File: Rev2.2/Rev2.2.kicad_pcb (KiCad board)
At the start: 4 copper layers, 91.8 x 94.5 mm, 119 parts, among them J1 Termination, J10 USART1, J11 3.3V power breakout, J12 5V power breakout, J13 AIN1, J15 USART6, J16 AIN2, J17 AIN3, J18 AIN4, J2 CAN2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

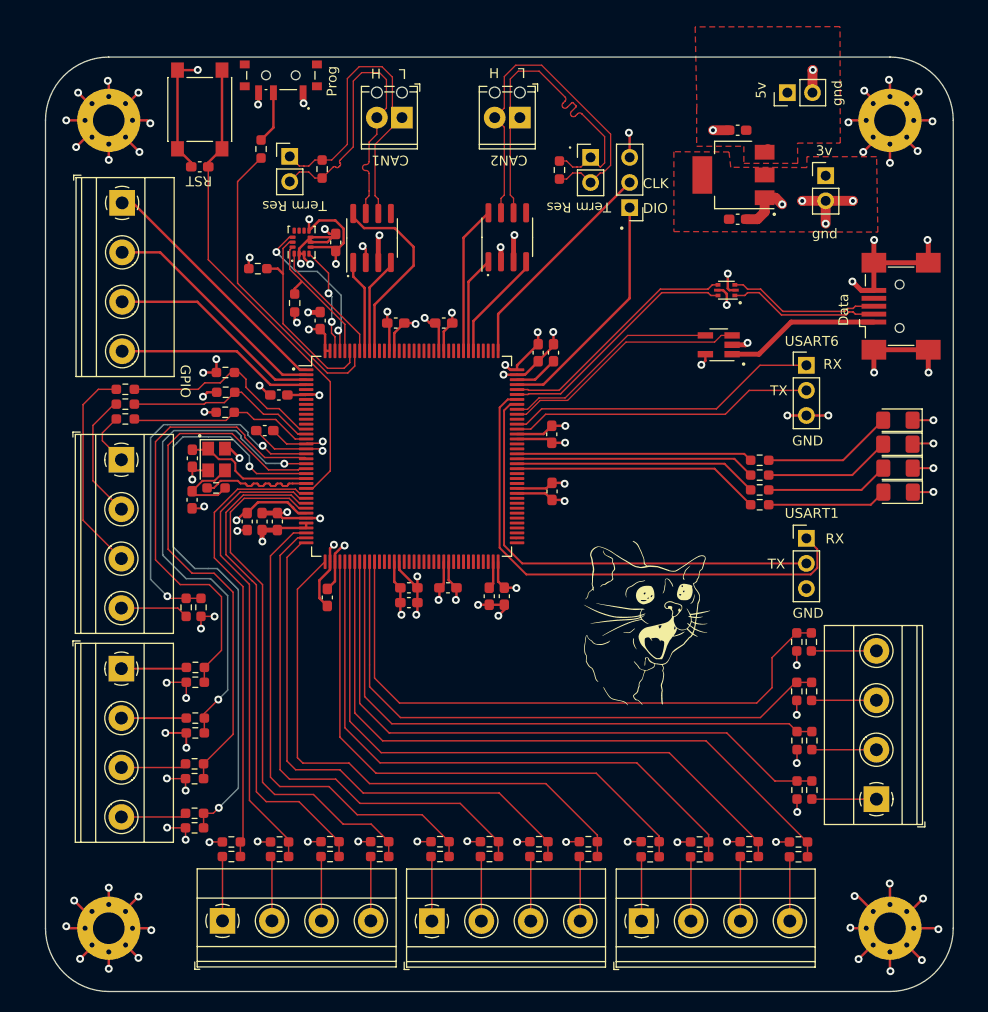
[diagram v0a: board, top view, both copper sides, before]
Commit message: changed layer stack up to sig,gnd,gnd, sig/power and routing according to the new stackup
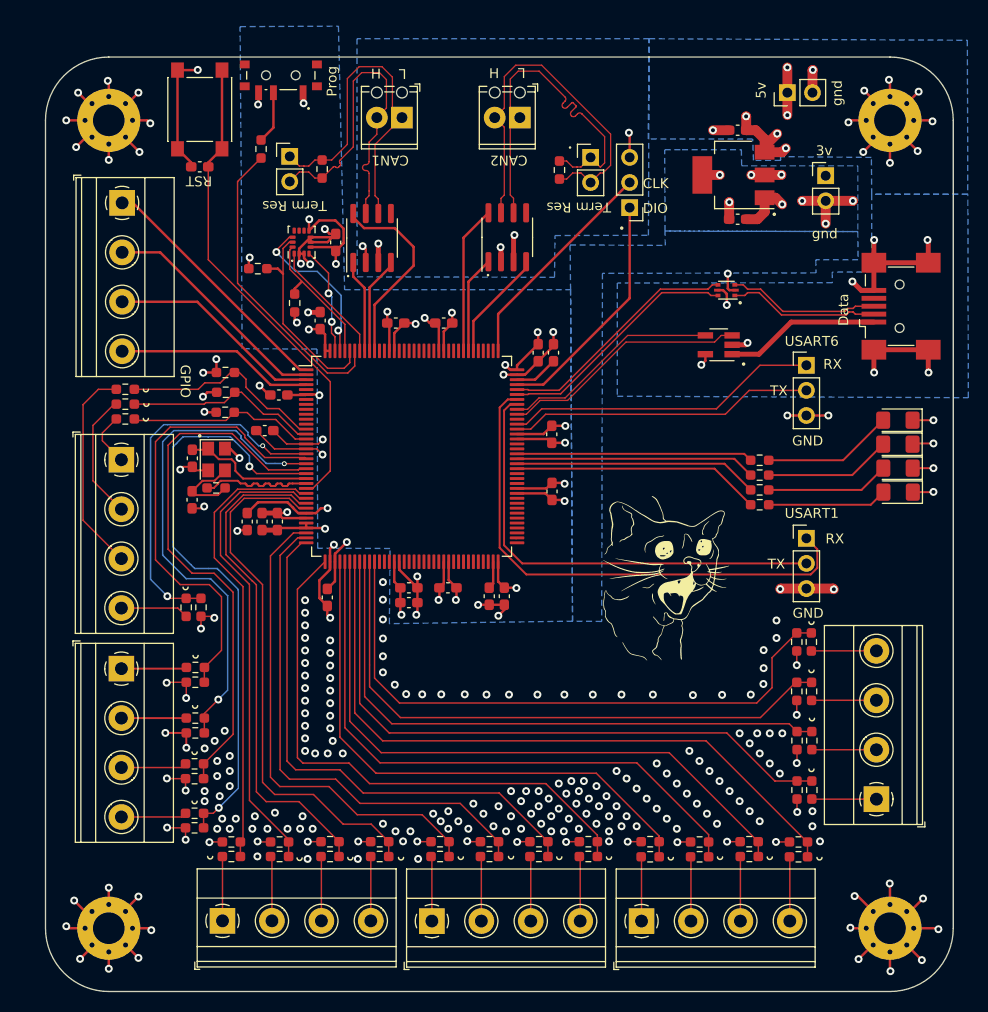
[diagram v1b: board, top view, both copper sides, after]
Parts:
- moved G*** 4.93 mm to (163.6, 111.0)
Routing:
- net +5V: track 9.48 -> 22.6 mm, vias 4 -> 9
- net +3.3V: track 91.0 -> 100.2 mm, vias 21 -> 25
- net GND: track 269.0 -> 274.5 mm, vias 109 -> 272
- added copper zone on B.Cu, net +3.3V
- added copper zone on B.Cu, net +5V
- removed copper zone on F.Cu, net +3.3V
- removed copper zone on F.Cu, net +5V
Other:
- board text added: "Analog section"
- board text added: "USB and UART"
- board text removed: "USB"

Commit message: added a usb C for power delivery and moved voltage regulator and readjusted the partial power plane to fit the USB C
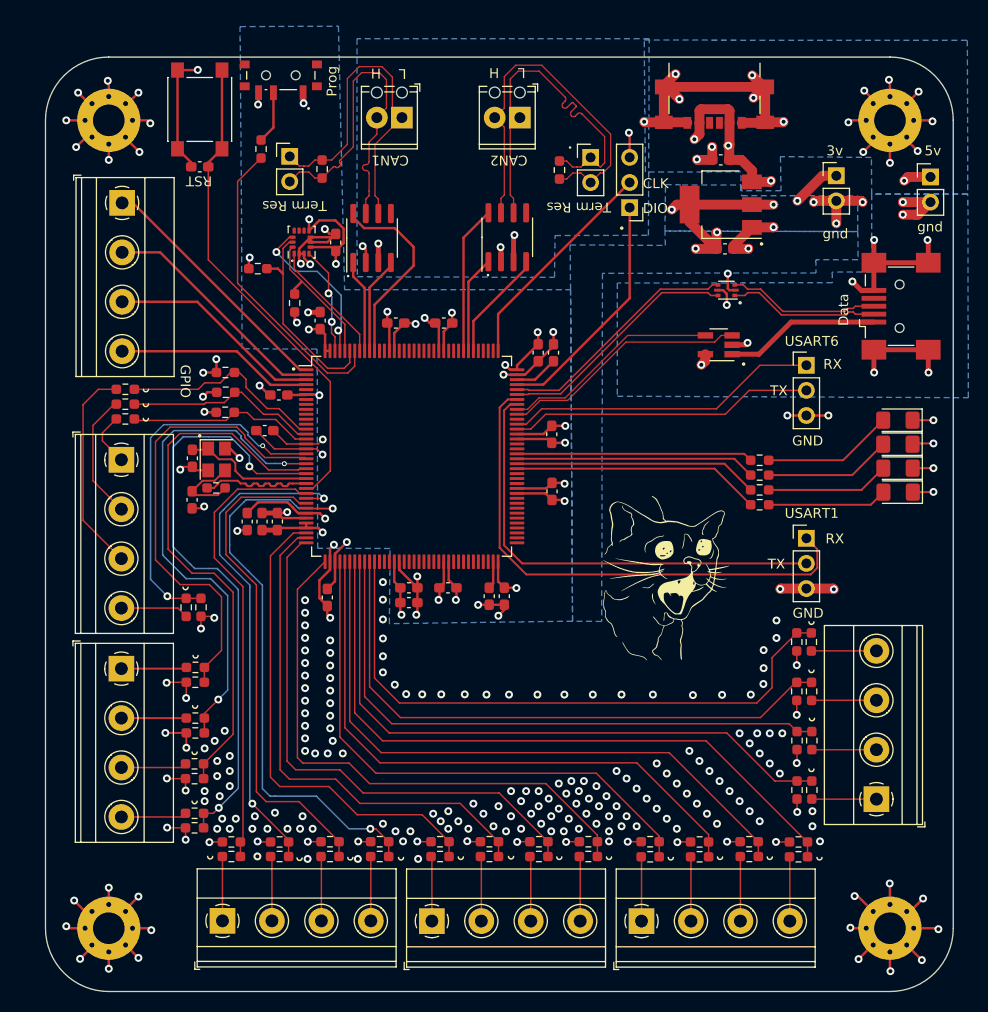
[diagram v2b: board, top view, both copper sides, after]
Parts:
- added J14: USB C PWR, Connector_USB:USB_C_Receptacle_GCT_USB4135-GF-A_6P_TopMnt_Horizontal, F.Cu at (168.7, 61.7)
- moved J12 16.8 mm to (190.5, 70.2), turned to 0 degrees
- moved C26 3.45 mm to (169.3, 68.5)
- moved C32 3.26 mm to (169.7, 77.5)
- moved U3 3.26 mm to (169.3, 73.0)
- moved J11 1.08 mm to (181.0, 70.1)
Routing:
- net GND: track 274.5 -> 313.9 mm, vias 272 -> 281
- net +3.3V: track 100.2 -> 118.2 mm, vias 25 -> 26
- net +5V: track 22.6 -> 28.2 mm, vias 9 -> 8
- net A12: track 54.1 -> 59.6 mm, vias 0 -> 2
- net A10: track 47.5 -> 51.0 mm, vias 0 -> 2

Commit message: added manufacturing files
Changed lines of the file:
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@@
       (outputformat 1)
       (mirror false)
-      (drillshape 1)
+      (drillshape 0)
       (scaleselection 1)
-      (outputdirectory "")
+      (outputdirectory "manufacturing/")
     )
   )
@@
     (fp_line (start 1.6 0.8) (end 1.6 -0.8)
       (stroke (width 0.1) (type solid)) (layer "F.Fab"))
-    (pad "1" smd roundrect (at -1.4875 0 180) (size 1.425 1.75) (layers "F.Cu" "F.Paste" "F.Mask") (roundrect_rratio 0.175439)
+    (pad "1" smd roundrect (at -1.4875 0 180) (size 1.425 1.75) (layers "F.Cu" "F.Paste" "F.Mask") (roundrect_rratio 0.1754392982)
       (net 2 "GND") (pinfunction "K") (pintype "passive"))
-    (pad "2" smd roundrect (at 1.4875 0 180) (size 1.425 1.75) (layers "F.Cu" "F.Paste" "F.Mask") (roundrect_rratio 0.175439)
+    (pad "2" smd roundrect (at 1.4875 0 180) (size 1.425 1.75) (layers "F.Cu" "F.Paste" "F.Mask") (roundrect_rratio 0.1754392982)
       (net 4 "Net-(D2-A)") (pinfunction "A") (pintype "passive"))
     (model "${KICAD6_3DMODEL_DIR}/LED_SMD.3dshapes/LED_1206_3216Metric.wrl"
@@
     (fp_line (start 1.6 0.8) (end 1.6 -0.8)
       (stroke (width 0.1) (type solid)) (layer "F.Fab"))
-    (pad "1" smd roundrect (at -1.4875 0 180) (size 1.425 1.75) (layers "F.Cu" "F.Paste" "F.Mask") (roundrect_rratio 0.175439)
+    (pad "1" smd roundrect (at -1.4875 0 180) (size 1.425 1.75) (layers "F.Cu" "F.Paste" "F.Mask") (roundrect_rratio 0.1754392982)
       (net 2 "GND") (pinfunction "K") (pintype "passive"))
-    (pad "2" smd roundrect (at 1.4875 0 180) (size 1.425 1.75) (layers "F.Cu" "F.Paste" "F.Mask") (roundrect_rratio 0.175439)
+    (pad "2" smd roundrect (at 1.4875 0 180) (size 1.425 1.75) (layers "F.Cu" "F.Paste" "F.Mask") (roundrect_rratio 0.1754392982)
       (net 5 "Net-(D3-A)") (pinfunction "A") (pintype "passive"))
     (model "${KICAD6_3DMODEL_DIR}/LED_SMD.3dshapes/LED_1206_3216Metric.wrl"
@@
     (fp_line (start 1.6 0.8) (end 1.6 -0.8)
       (stroke (width 0.1) (type solid)) (layer "F.Fab"))
-    (pad "1" smd roundrect (at -1.4875 0 180) (size 1.425 1.75) (layers "F.Cu" "F.Paste" "F.Mask") (roundrect_rratio 0.175439)
+    (pad "1" smd roundrect (at -1.4875 0 180) (size 1.425 1.75) (layers "F.Cu" "F.Paste" "F.Mask") (roundrect_rratio 0.1754392982)
       (net 2 "GND") (pinfunction "K") (pintype "passive"))
-    (pad "2" smd roundrect (at 1.4875 0 180) (size 1.425 1.75) (layers "F.Cu" "F.Paste" "F.Mask") (roundrect_rratio 0.175439)
+    (pad "2" smd roundrect (at 1.4875 0 180) (size 1.425 1.75) (layers "F.Cu" "F.Paste" "F.Mask") (roundrect_rratio 0.1754392982)
       (net 6 "Net-(D4-A)") (pinfunction "A") (pintype "passive"))
     (model "${KICAD6_3DMODEL_DIR}/LED_SMD.3dshapes/LED_1206_3216Metric.wrl"
@@
     (fp_line (start 1.6 0.8) (end 1.6 -0.8)
       (stroke (width 0.1) (type solid)) (layer "F.Fab"))
-    (pad "1" smd roundrect (at -1.4875 0 180) (size 1.425 1.75) (layers "F.Cu" "F.Paste" "F.Mask") (roundrect_rratio 0.175439)
+    (pad "1" smd roundrect (at -1.4875 0 180) (size 1.425 1.75) (layers "F.Cu" "F.Paste" "F.Mask") (roundrect_rratio 0.1754392982)
       (net 2 "GND") (pinfunction "K") (pintype "passive"))
-    (pad "2" smd roundrect (at 1.4875 0 180) (size 1.425 1.75) (layers "F.Cu" "F.Paste" "F.Mask") (roundrect_rratio 0.175439)
+    (pad "2" smd roundrect (at 1.4875 0 180) (size 1.425 1.75) (layers "F.Cu" "F.Paste" "F.Mask") (roundrect_rratio 0.1754392982)
       (net 3 "Net-(D1-A)") (pinfunction "A") (pintype "passive"))
     (model "${KICAD6_3DMODEL_DIR}/LED_SMD.3dshapes/LED_1206_3216Metric.wrl"
@@
   (gr_circle (center 168.9608 138.7348) (end 168.9608 138.7348)
     (stroke (width 0.15) (type default)) (fill none) (layer "F.SilkS"))
+  (gr_line (start 189.992 98.552) (end 190.4492 98.552)
+    (stroke (width 0.15) (type default)) (layer "F.SilkS"))
   (gr_circle (center 154.05 67.25) (end 154 67.25)
     (stroke (width 0.15) (type default)) (fill none) (layer "F.SilkS"))
@@
   (gr_arc (start 164.4904 139.0396) (mid 164.2364 139.2936) (end 163.9824 139.0396)
     (stroke (width 0.15) (type default)) (layer "F.SilkS"))
+  (gr_line (start 189.9793 96.139) (end 190.4619 96.139)
+    (stroke (width 0.15) (type default)) (layer "F.SilkS"))
   (gr_arc (start 116.332 128.3716) (mid 116.078 128.6256) (end 115.824 128.3716)
     (stroke (width 0.15) (type default)) (layer "F.SilkS"))
@@
   (gr_circle (center 117.3988 138.684) (end 117.3988 138.684)
     (stroke (width 0.15) (type default)) (fill none) (layer "F.SilkS"))
+  (gr_line (start 189.9793 100.9904) (end 190.4619 100.9904)
+    (stroke (width 0.15) (type default)) (layer "F.SilkS"))
   (gr_circle (center 147.828 138.684) (end 147.828 138.684)
     (stroke (width 0.15) (type default)) (fill none) (layer "F.SilkS"))
@@
   (gr_circle (center 164.4904 138.7856) (end 164.4904 138.7856)
     (stroke (width 0.15) (type default)) (fill none) (layer "F.SilkS"))
+  (gr_line (start 189.992 93.726) (end 190.4746 93.726)
+    (stroke (width 0.15) (type default)) (layer "F.SilkS"))
   (gr_arc (start 143.256 138.9888) (mid 143.002 139.2428) (end 142.748 138.9888)
     (stroke (width 0.15) (type default)) (layer "F.SilkS"))

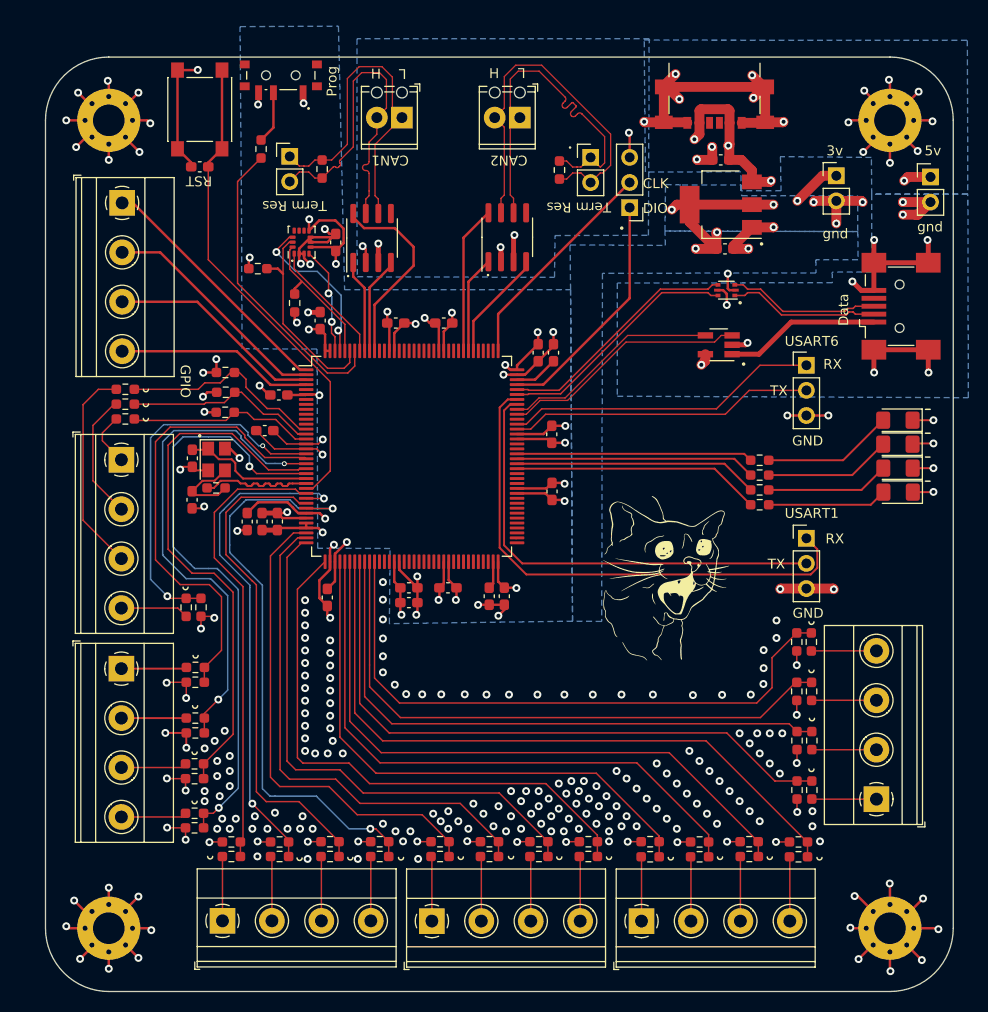
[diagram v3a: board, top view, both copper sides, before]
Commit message: updated gerber files to reflect some partial power plane adjustments
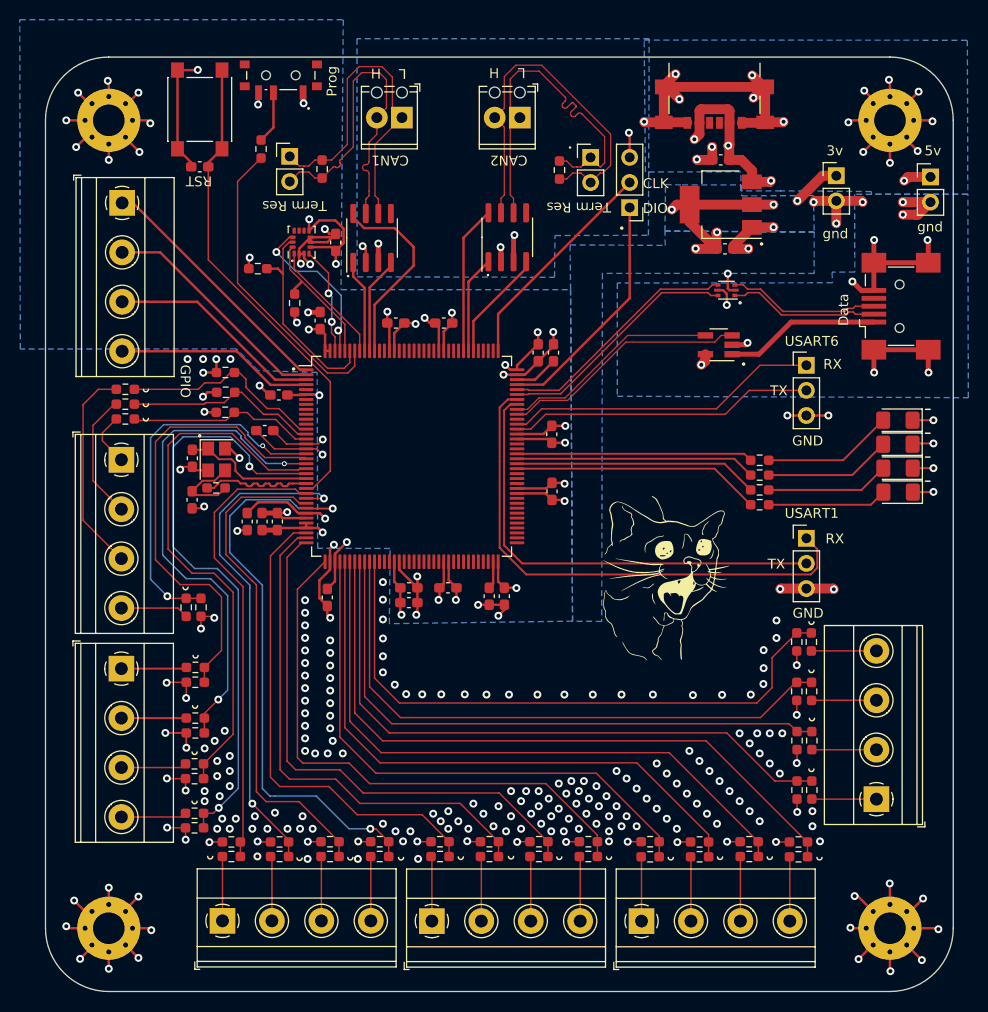
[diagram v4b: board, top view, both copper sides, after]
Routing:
- net GND: vias 281 -> 284
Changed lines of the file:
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@@
   (via (at 147.875 122.575) (size 0.8) (drill 0.4) (layers "F.Cu" "B.Cu") (net 2))
   (via (at 118.364 129.286) (size 0.8) (drill 0.4) (layers "F.Cu" "B.Cu") (net 2))
+  (via (at 119.7102 88.646) (size 0.8) (drill 0.4) (layers "F.Cu" "B.Cu") (net 2))
   (via (at 179.324 137.414) (size 0.8) (drill 0.4) (layers "F.Cu" "B.Cu") (net 2))
   (via (at 137 114.5) (size 0.8) (drill 0.4) (layers "F.Cu" "B.Cu") (net 2))
@@
   (via (at 119.634 128.778) (size 0.8) (drill 0.4) (layers "F.Cu" "B.Cu") (net 2))
   (via (at 159.25 122.575) (size 0.8) (drill 0.4) (layers "F.Cu" "B.Cu") (net 2))
+  (via (at 116.9416 88.646) (size 0.8) (drill 0.4) (layers "F.Cu" "B.Cu") (net 2))
   (via (at 142.748 135.382) (size 0.8) (drill 0.4) (layers "F.Cu" "B.Cu") (net 2))
   (via (at 127.254 114.3) (size 0.8) (drill 0.4) (layers "F.Cu" "B.Cu") (net 2))
@@
   (via (at 180.975 74.93) (size 0.8) (drill 0.4) (layers "F.Cu" "B.Cu") (net 2))
   (via (at 146.812 133.858) (size 0.8) (drill 0.4) (layers "F.Cu" "B.Cu") (net 2))
+  (via (at 115.3668 88.646) (size 0.8) (drill 0.4) (layers "F.Cu" "B.Cu") (net 2))
   (via (at 119.634 131.826) (size 0.8) (drill 0.4) (layers "F.Cu" "B.Cu") (net 2))
   (via (at 155.956 133.096) (size 0.8) (drill 0.4) (layers "F.Cu" "B.Cu") (net 2))
@@
     (polygon
       (pts
-        (xy 130.625 54.975)
-        (xy 131.25 81.625)
+        (xy 131.1148 54.3306)
+        (xy 130.8862 81.625)
         (xy 154.1 81.625)
         (xy 154.3 115.15)
@@
         (xy 135.85 107.8)
         (xy 128.525 107.775)
-        (xy 128.475 90.075)
-        (xy 128.45 87.625)
-        (xy 120.875 87.6)
-        (xy 120.825 74)
-        (xy 120.675 55.025)
+        (xy 128.475 89.9922)
+        (xy 122.5042 89.8144)
+        (xy 120.2944 87.6046)
+        (xy 98.4504 87.63)
+        (xy 98.3996 54.3306)
       )
     )
@@
         (xy 194.225 56.4)
         (xy 194.275 71.975)
-        (xy 184.55 71.975)
-        (xy 184.525 68.25)
-        (xy 175.325 68.175)
+        (xy 184.531 71.975)
+        (xy 184.525 71.7044)
+        (xy 175.325 71.6294)
         (xy 175.387 71.628)
         (xy 171.323 71.628)
@@
         (xy 171.375 71.031)
         (xy 171.4 72.136)
-        (xy 183.134 72.136)
-        (xy 183.15 75.75)
+        (xy 178.6636 72.1106)
+        (xy 178.7398 75.7936)
         (xy 163.65 75.7)
         (xy 163.703 70.993)
@@
     (polygon
       (pts
-        (xy 184.55 71.975)
-        (xy 184.575 79.85)
+        (xy 182.8228 71.975)
+        (xy 182.8478 79.85)
         (xy 180.55 79.85)
         (xy 180.575 80.925)
@@
         (xy 163.675 77.15)
         (xy 163.65 75.7)
-        (xy 183.15 75.75)
-        (xy 183.175 78.6)
-        (xy 178.9 78.6)
-        (xy 178.925 79.925)
+        (xy 178.7398 75.7936)
+        (xy 178.7398 78.6384)
+        (xy 178.7222 78.6762)
+        (xy 178.7398 79.9846)
         (xy 157.325 79.975)
         (xy 157.25 115.175)
